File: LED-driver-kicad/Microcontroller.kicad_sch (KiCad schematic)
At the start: 11 parts, among them J2 Conn_01x02_Socket, J3 Conn_01x05_Socket, SW1 SW_SPDT, U6 PIC16F18026-ISL

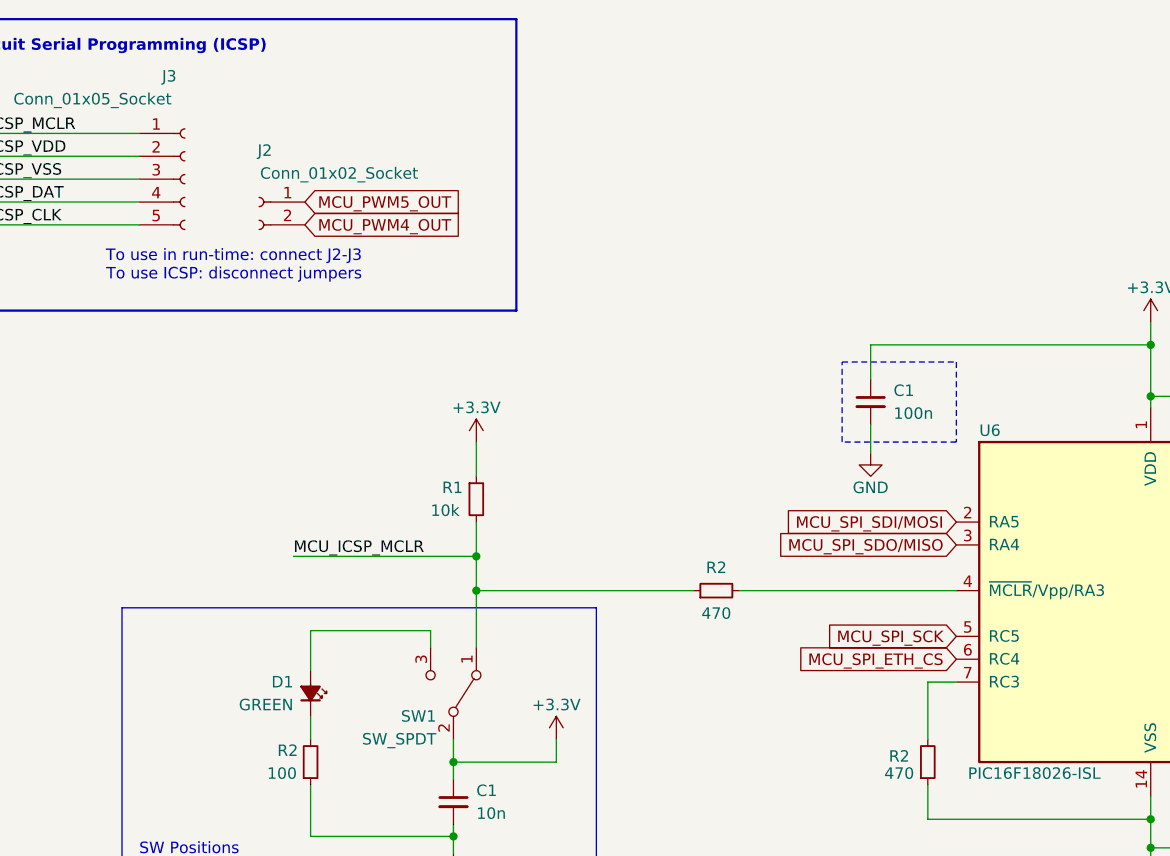
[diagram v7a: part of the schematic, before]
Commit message: update component designators
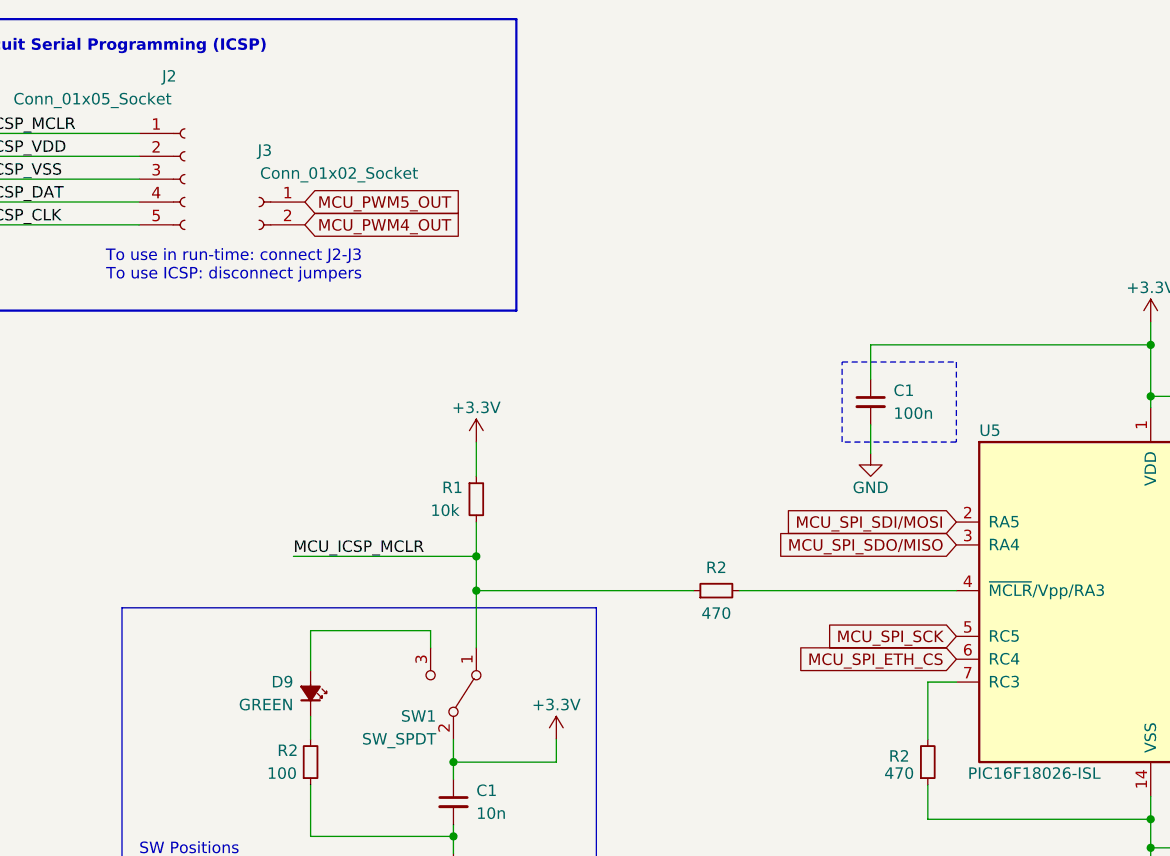
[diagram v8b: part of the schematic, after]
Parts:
- renumbered D1 to D9, J3 to J2, J2 to J3, U6 to U5
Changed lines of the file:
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@@
         )
         (path "/2b071084-2ab6-4896-84cc-45b211479417/9127cd83-cae7-424d-ad3b-8a9e0439da28"
-          (reference "R3") (unit 1)
+          (reference "R23") (unit 1)
         )
       )
@@
         )
         (path "/2b071084-2ab6-4896-84cc-45b211479417/9127cd83-cae7-424d-ad3b-8a9e0439da28"
-          (reference "C29") (unit 1)
+          (reference "C19") (unit 1)
         )
       )
@@
         )
         (path "/2b071084-2ab6-4896-84cc-45b211479417/9127cd83-cae7-424d-ad3b-8a9e0439da28"
-          (reference "R2") (unit 1)
+          (reference "R22") (unit 1)
         )
       )
@@
         )
         (path "/2b071084-2ab6-4896-84cc-45b211479417/9127cd83-cae7-424d-ad3b-8a9e0439da28"
-          (reference "#PWR035") (unit 1)
+          (reference "#PWR032") (unit 1)
         )
       )
@@
   (symbol (lib_id "power:GND") (at 154.94 113.665 0) (unit 1)
     (in_bom yes) (on_board yes) (dnp no)
-    (property "Reference" "#PWR039" (at 154.94 120.015 0)
+    (property "Reference" "#PWR033" (at 154.94 120.015 0)
       (effects (font (size 1.27 1.27)) hide)
     )
@@
       (project "LED-driver-kicad"
         (path "/2b071084-2ab6-4896-84cc-45b211479417/9127cd83-cae7-424d-ad3b-8a9e0439da28"
-          (reference "#PWR039") (unit 1)
+          (reference "#PWR033") (unit 1)
         )
       )
@@
         )
         (path "/2b071084-2ab6-4896-84cc-45b211479417/9127cd83-cae7-424d-ad3b-8a9e0439da28"
-          (reference "#PWR036") (unit 1)
+          (reference "#PWR031") (unit 1)
         )
       )
@@
         )
         (path "/2b071084-2ab6-4896-84cc-45b211479417/9127cd83-cae7-424d-ad3b-8a9e0439da28"
-          (reference "R1") (unit 1)
+          (reference "R21") (unit 1)
         )
       )
@@
   (symbol (lib_id "power:GND") (at 123.825 67.31 0) (unit 1)
     (in_bom yes) (on_board yes) (dnp no)
-    (property "Reference" "#PWR018" (at 123.825 73.66 0)
+    (property "Reference" "#PWR030" (at 123.825 73.66 0)
       (effects (font (size 1.27 1.27)) hide)
     )
@@
       (project "LED-driver-kicad"
         (path "/2b071084-2ab6-4896-84cc-45b211479417/9127cd83-cae7-424d-ad3b-8a9e0439da28"
-          (reference "#PWR018") (unit 1)
+          (reference "#PWR030") (unit 1)
         )
       )
@@
   (symbol (lib_id "Device:LED_Small_Filled") (at 61.595 93.98 270) (mirror x) (unit 1)
     (in_bom yes) (on_board yes) (dnp no)
-    (property "Reference" "D1" (at 59.69 92.71 90)
+    (property "Reference" "D9" (at 59.69 92.71 90)
       (effects (font (size 1.27 1.27)) (justify right))
     )
@@
       (project "LED-driver-kicad"
         (path "/2b071084-2ab6-4896-84cc-45b211479417/9127cd83-cae7-424d-ad3b-8a9e0439da28"
-          (reference "D1") (unit 1)
+          (reference "D9") (unit 1)
         )
       )
@@
   (symbol (lib_id "Connector:Conn_01x05_Socket") (at 47.625 36.83 0) (unit 1)
     (in_bom yes) (on_board yes) (dnp no)
-    (property "Reference" "J3" (at 45.085 25.4 0)
+    (property "Reference" "J2" (at 45.085 25.4 0)
       (effects (font (size 1.27 1.27)) (justify left))
     )
@@
       (project "LED-driver-kicad"
         (path "/2b071084-2ab6-4896-84cc-45b211479417/9127cd83-cae7-424d-ad3b-8a9e0439da28"
-          (reference "J3") (unit 1)
+          (reference "J2") (unit 1)
         )
       )
@@
         )
         (path "/2b071084-2ab6-4896-84cc-45b211479417/9127cd83-cae7-424d-ad3b-8a9e0439da28"
-          (reference "C1") (unit 1)
+          (reference "C20") (unit 1)
         )
       )
@@
         )
         (path "/2b071084-2ab6-4896-84cc-45b211479417/9127cd83-cae7-424d-ad3b-8a9e0439da28"
-          (reference "#PWR02") (unit 1)
+          (reference "#PWR029") (unit 1)
         )
       )
@@
         )
         (path "/2b071084-2ab6-4896-84cc-45b211479417/9127cd83-cae7-424d-ad3b-8a9e0439da28"
-          (reference "R40") (unit 1)
+          (reference "R24") (unit 1)
         )
       )
@@
   (symbol (lib_id "Connector:Conn_01x02_Socket") (at 55.88 39.37 0) (mirror y) (unit 1)
     (in_bom yes) (on_board yes) (dnp no)
-    (property "Reference" "J2" (at 56.515 33.655 0)
+    (property "Reference" "J3" (at 56.515 33.655 0)
       (effects (font (size 1.27 1.27)))
     )
@@
       (project "LED-driver-kicad"
         (path "/2b071084-2ab6-4896-84cc-45b211479417/9127cd83-cae7-424d-ad3b-8a9e0439da28"
-          (reference "J2") (unit 1)
+          (reference "J3") (unit 1)
         )
       )
@@
   (symbol (lib_id "MCU_Microchip_PIC1616f1829-ISL:PIC16F18026-ISL") (at 154.94 85.09 0) (unit 1)
     (in_bom yes) (on_board yes) (dnp no)
-    (property "Reference" "U6" (at 135.89 64.77 0)
+    (property "Reference" "U5" (at 135.89 64.77 0)
       (effects (font (size 1.27 1.27)) (justify left))
     )
@@
       (project "LED-driver-kicad"
         (path "/2b071084-2ab6-4896-84cc-45b211479417/9127cd83-cae7-424d-ad3b-8a9e0439da28"
-          (reference "U6") (unit 1)
+          (reference "U5") (unit 1)
         )
       )
@@
   (symbol (lib_id "power:+3.3V") (at 154.94 52.705 0) (unit 1)
     (in_bom yes) (on_board yes) (dnp no)
-    (property "Reference" "#PWR017" (at 154.94 56.515 0)
+    (property "Reference" "#PWR028" (at 154.94 56.515 0)
       (effects (font (size 1.27 1.27)) hide)
     )
@@
       (project "LED-driver-kicad"
         (path "/2b071084-2ab6-4896-84cc-45b211479417/9127cd83-cae7-424d-ad3b-8a9e0439da28"
-          (reference "#PWR017") (unit 1)
-        )
-      )
+          (reference "#PWR028") (unit 1)
+        )
+      )
